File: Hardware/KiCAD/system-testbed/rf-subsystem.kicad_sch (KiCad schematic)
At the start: 86 parts, among them P1 SMA, P2 SMA, SW3 SKY13330-397LF, SW4 SKY13330-397LF, U2 CC1200RHBR, U3 LP5907MFX-2.5, U4 TXS0101DBV, X5 40 MHz

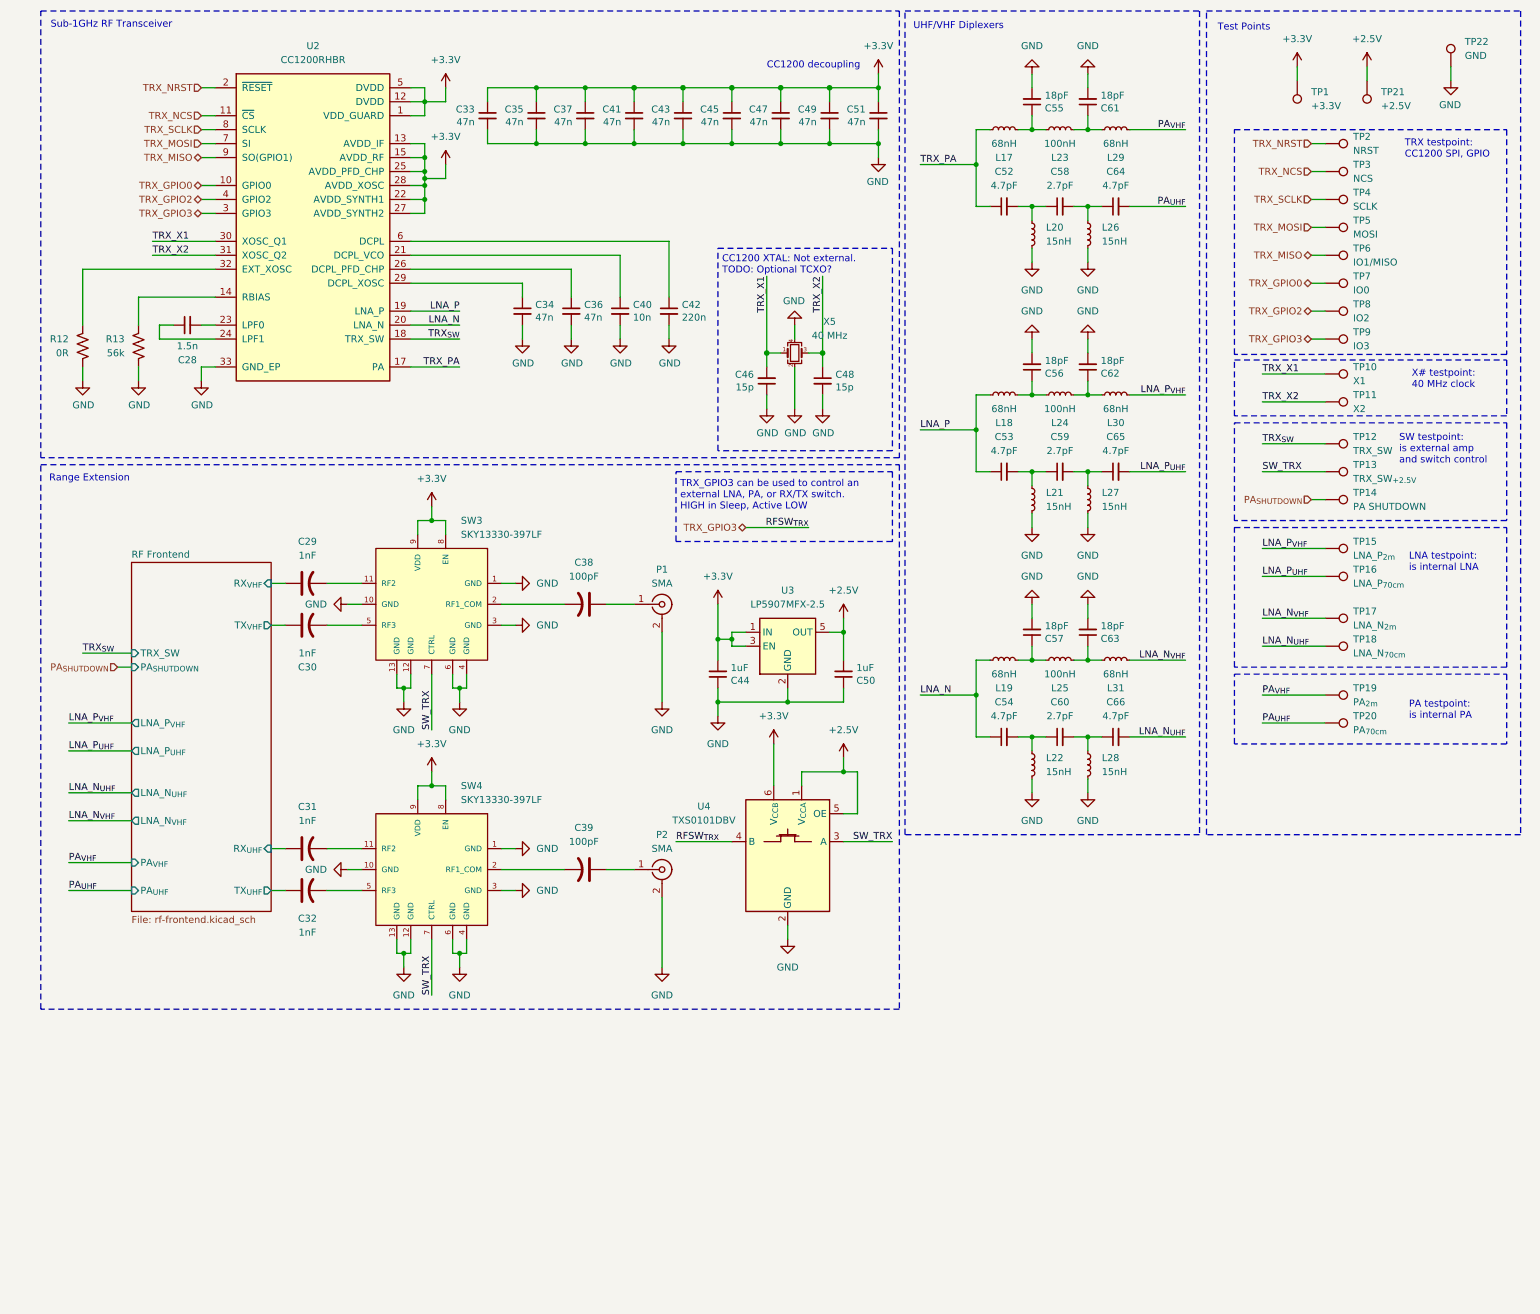
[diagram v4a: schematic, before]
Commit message: feat: separate RF subsystems for testing using SMA edge launches in testbed KiCAD project #65 #34 #45
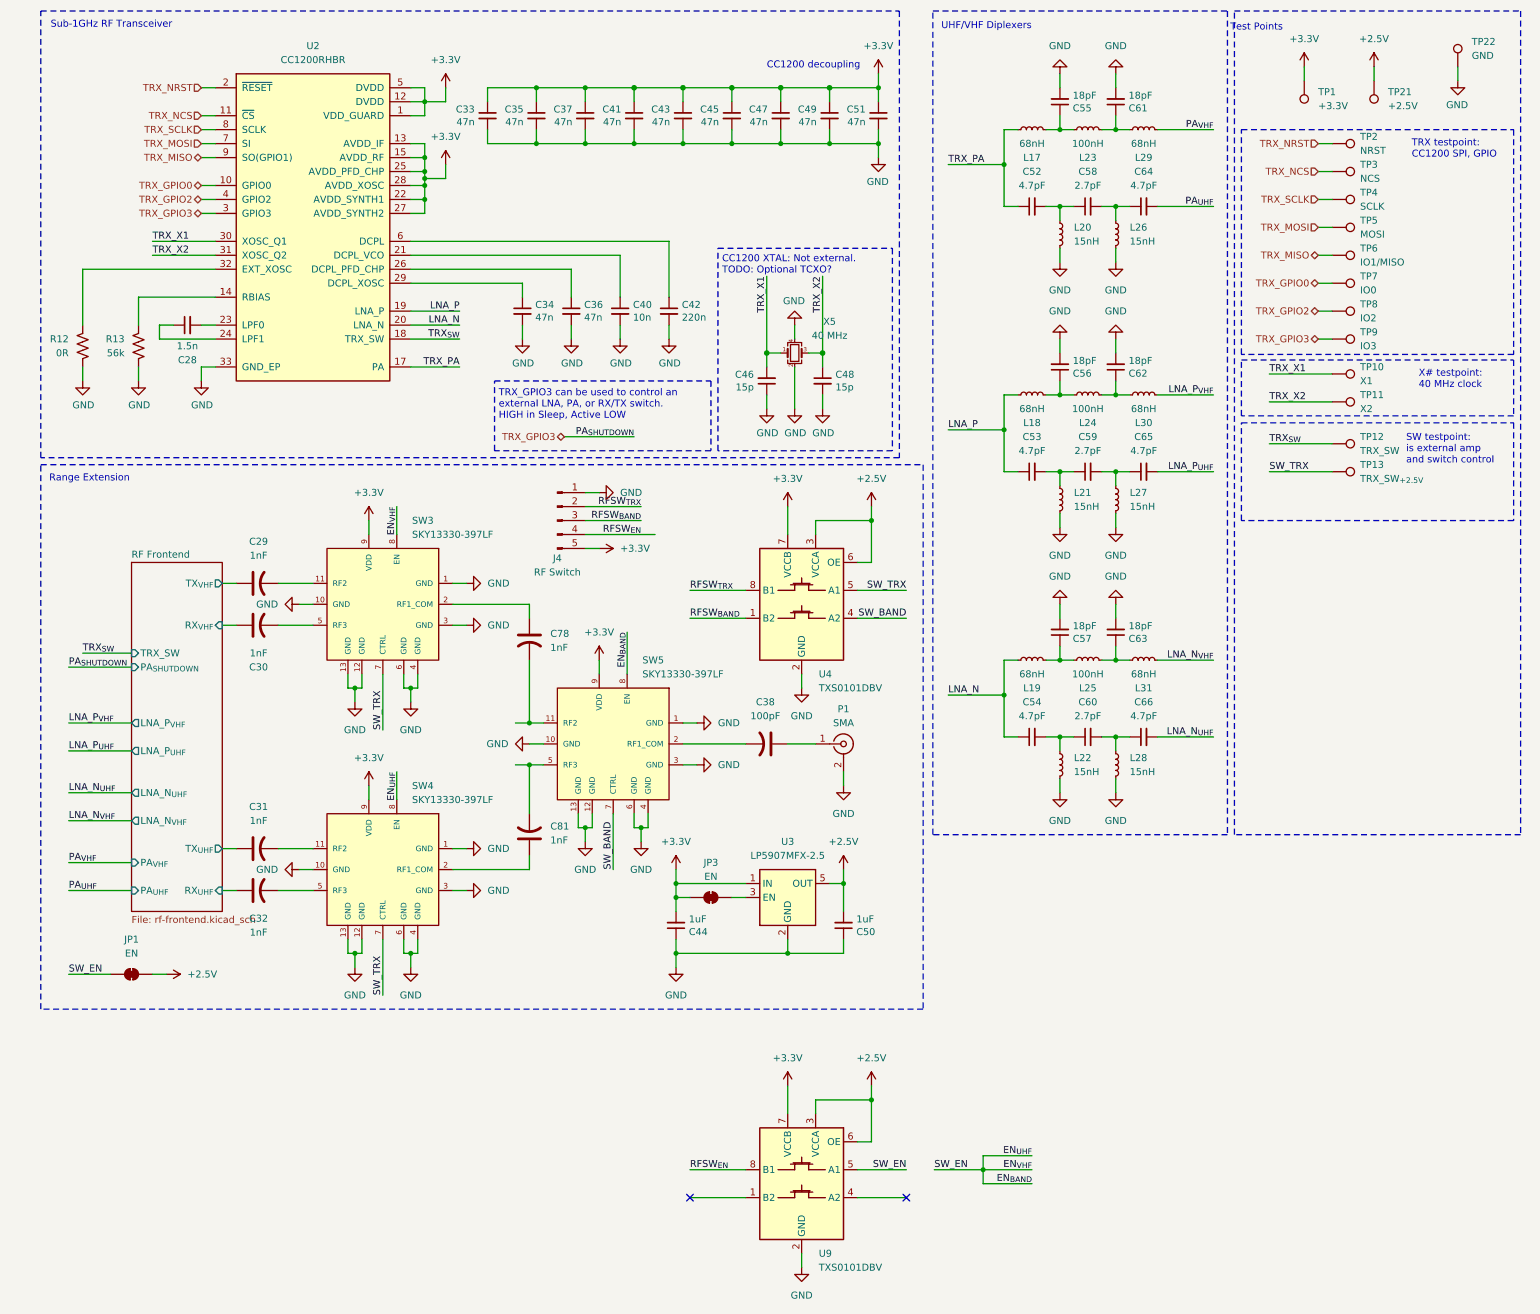
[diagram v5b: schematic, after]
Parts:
- removed C39: 100pF, Capacitor_SMD:C_0402_1005Metric, symbol Device:C_US
- removed P2: SMA, Connector_Coaxial:SMA_Amphenol_901-144_Vertical, symbol Connector:Conn_Coaxial
- removed TP14: PA SHUTDOWN, TestPoint:TestPoint_Pad_D1.0mm, symbol Connector:TestPoint
- removed TP15: LNA_P_{2m}, TestPoint:TestPoint_Pad_D1.0mm, symbol Connector:TestPoint
- removed TP16: LNA_P_{70cm}, TestPoint:TestPoint_Pad_D1.0mm, symbol Connector:TestPoint
- removed TP17: LNA_N_{2m}, TestPoint:TestPoint_Pad_D1.0mm, symbol Connector:TestPoint
- removed TP18: LNA_N_{70cm}, TestPoint:TestPoint_Pad_D1.0mm, symbol Connector:TestPoint
- removed TP19: PA_{2m}, TestPoint:TestPoint_Pad_D1.0mm, symbol Connector:TestPoint
- removed TP20: PA_{70cm}, TestPoint:TestPoint_Pad_D1.0mm, symbol Connector:TestPoint
- added C78, C81: 1nF, Capacitor_SMD:C_0402_1005Metric, symbol Device:C_US
- added J4: RF Switch, Connector_PinHeader_2.54mm:PinHeader_1x05_P2.54mm_Vertical, symbol Connector:Conn_01x05_Pin
- added JP1, JP3: EN, Jumper:SolderJumper-2_P1.3mm_Open_RoundedPad1.0x1.5mm, symbol Jumper:SolderJumper_2_Bridged
- added SW5: SKY13330-397LF, capstone-project:SKY13330-397LF, symbol capstone-project:SKY13330-397LF
- added U9: TXS0101DBV, Package_SO:VSSOP-8_2.3x2mm_P0.5mm, symbol Logic_LevelTranslator:TXS0102DCU
- C54: footprint Capacitor_SMD:C_0603_1608Metric -> Capacitor_SMD:C_0402_1005Metric
- U4: footprint Package_TO_SOT_SMD:SOT-23-6 -> Package_SO:VSSOP-8_2.3x2mm_P0.5mm; symbol Logic_LevelTranslator:TXS0101DBV -> Logic_LevelTranslator:TXS0102DCU
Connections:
- net +2.5V: now also U4.3 (VCCA), U4.6 (OE), JP1.1 (A), U9.3 (VCCA), U9.6 (OE); no longer U4.1 (V_{CCA}), U4.5 (OE)
- net +3.3V: now also U4.7 (VCCB), J4.5 (Pin_5), JP3.1 (A), SW5.9 (VDD), U9.7 (VCCB); no longer SW3.8 (EN), SW4.8 (EN), U3.3 (EN), U4.6 (V_{CCB})
- net GND: now also J4.1 (Pin_1), SW5.1 (GND), SW5.10 (GND), SW5.12 (GND), SW5.13 (GND), SW5.3 (GND), SW5.4 (GND), SW5.6 (GND), U9.2 (GND)
- net RF Frontend/RX_{UHF}: now also C32.1; no longer C31.1
- net RF Frontend/RX_{VHF}: now also C30.1; no longer C29.1
- net RF Frontend/TX_{UHF}: now also C31.1; no longer C32.1
- net RF Frontend/TX_{VHF}: now also C29.1; no longer C30.1
- net SW_TRX: now also U4.5 (A1); no longer U4.3 (A)
- net TRX_GPIO3: no longer U4.4 (B)
- net at SW3.2 (RF1_COM): now also C78.1; no longer C38.2
- net at SW4.2 (RF1_COM): now also C81.1
- new net: JP3.2 (B), U3.3 (EN)
- new net: C78.2, SW5.11 (RF2)
- new net: C38.2, SW5.2 (RF1_COM)
- new net: C81.2, SW5.5 (RF3)
- new net EN_{BAND}: JP1.2 (B), SW3.8 (EN), SW4.8 (EN), SW5.8 (EN), U9.5 (A1)
- new net RFSW_{BAND}: J4.3 (Pin_3), U4.1 (B2)
- new net RFSW_{EN}: J4.4 (Pin_4), U9.8 (B1)
- new net RFSW_{TRX}: J4.2 (Pin_2), U4.8 (B1)
- new net SW_BAND: SW5.7 (CTRL), U4.4 (A2)
- no-connect marks 0 -> 2
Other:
- note removed: "LNA testpoint: is internal LNA"
- note removed: "PA testpoint: is internal PA"
- moved on the sheet: C29, C30, C31, C32, C38, C44, C50, C52, C53, C54, C55, C56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
